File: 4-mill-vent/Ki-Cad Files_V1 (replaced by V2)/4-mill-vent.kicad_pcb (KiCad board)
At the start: 2 copper layers, 76.2 x 47.6 mm, 71 parts, among them J1 Fan, J2 Buzzer, J3 Power, J4 ICSP, Q3 PZT3904, Q4 PZT3904, Q5 TSM480P06CP, Q6 MMBT3904, SW1 Power_off, SW2 Power_On, SW3 Fan_Down, SW4 Fan_Up, U1 LM321, U2 ATmega328P-AU, U3 TPSM84212EAB, U4 LM1117-5.0, Y1 16.000MHZ

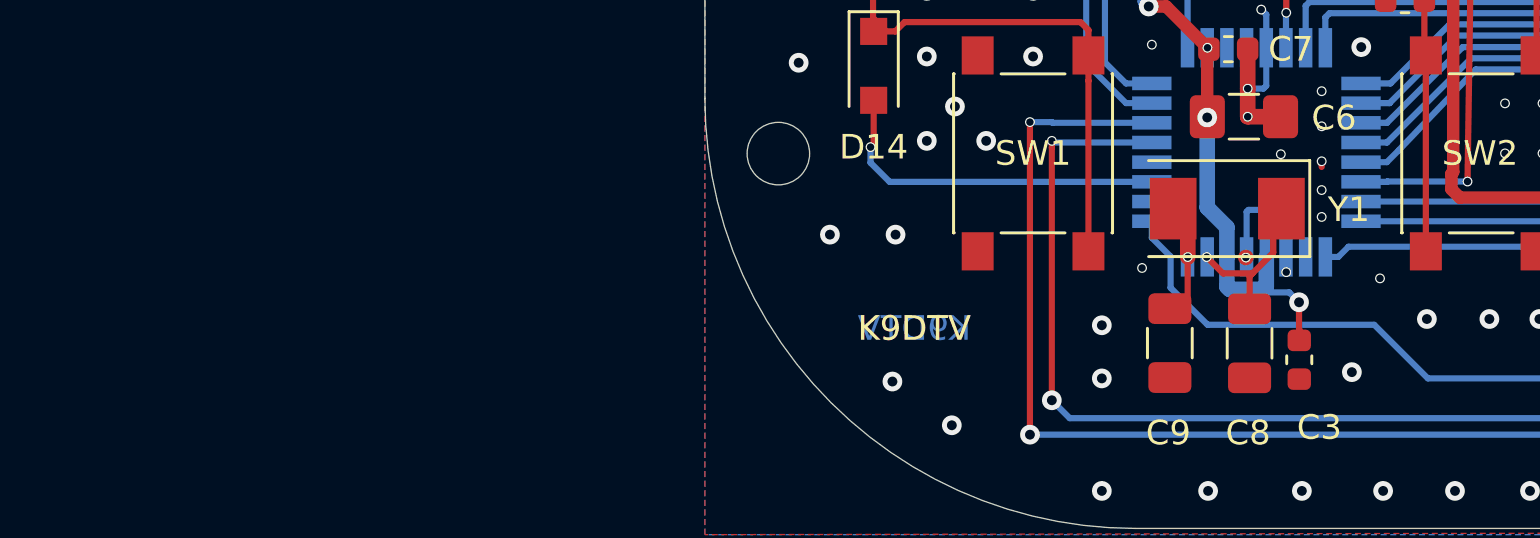
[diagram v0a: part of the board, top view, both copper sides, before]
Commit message: Last Update USE V2
Board test complete, all slikscreen error are fixed in v2, Full use of opamp for battery monitoring.
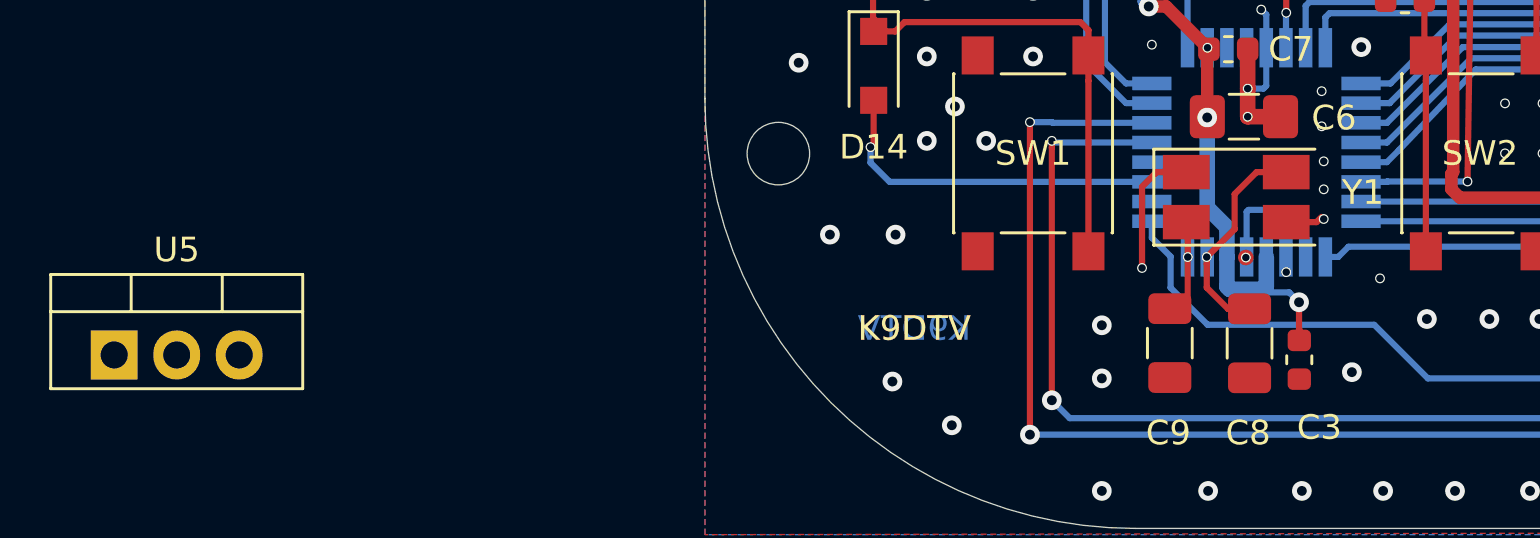
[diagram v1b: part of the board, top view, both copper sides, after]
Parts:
- added U5: LM317_TO-220, Package_TO_SOT_THT:TO-220-3_Vertical, F.Cu at (75.2, 108.9)
- Y1: value 16.000MHZ -> Crystal_16MHZ; footprint Crystal:Crystal_SMD_0603-2Pin_6.0x3.5mm -> Crystal:Crystal_SMD_0603-4Pin_6.0x3.5mm
- moved Y1 0.59 mm to (120.8, 102.5), turned to 0 degrees
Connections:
- Y1 pad 1: Net-(C8-Pad1) -> Net-(C9-Pad1)
- Y1 pad 2: Net-(C9-Pad1) -> GND
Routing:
- net GND: track 19.1 -> 25.7 mm, vias 174 -> 173
- net Net-(C8-Pad1): track 7.88 -> 8.83 mm
- net Net-(C9-Pad1): track 4.39 -> 3.62 mm
